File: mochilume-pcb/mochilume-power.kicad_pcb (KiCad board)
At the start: 2 copper layers, 90 x 60.1 mm, 28 parts, among them U1 llcc68_custom_module

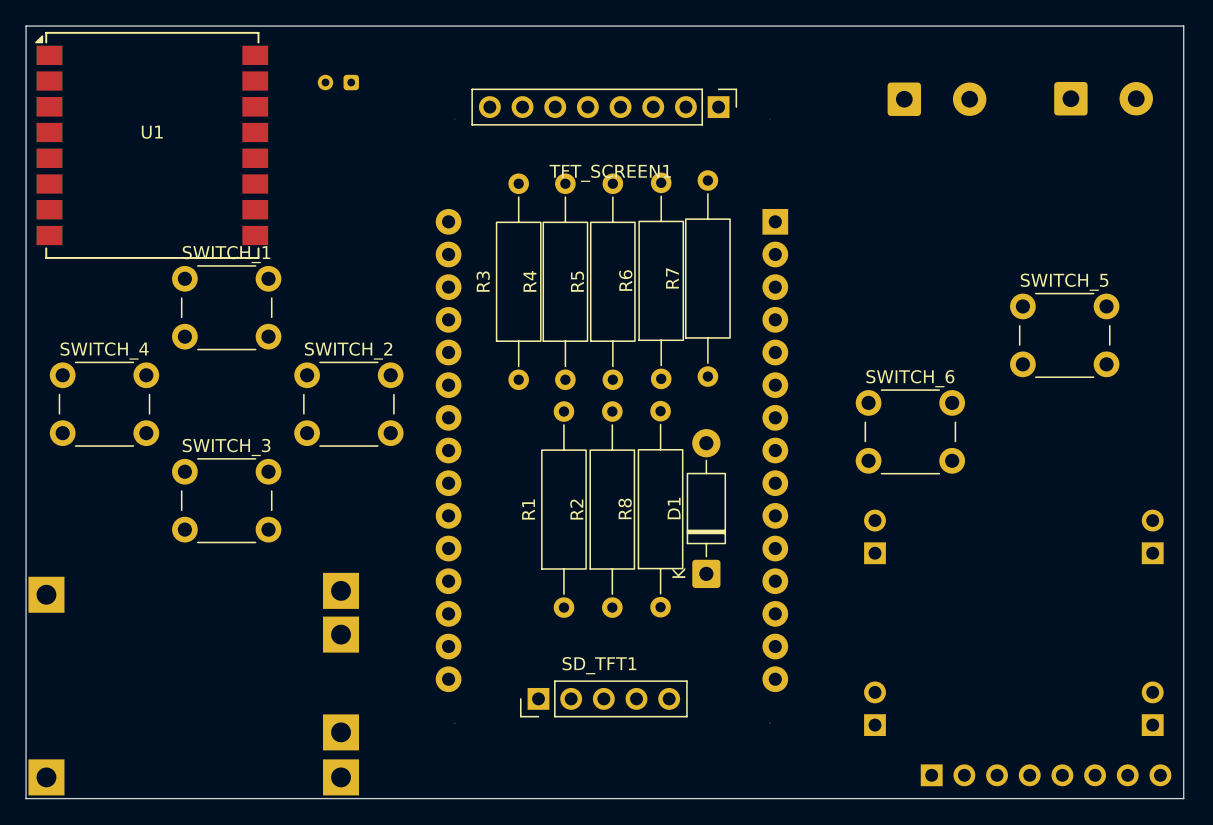
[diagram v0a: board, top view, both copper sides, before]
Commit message: feat pcb: add via tracking to power pcb
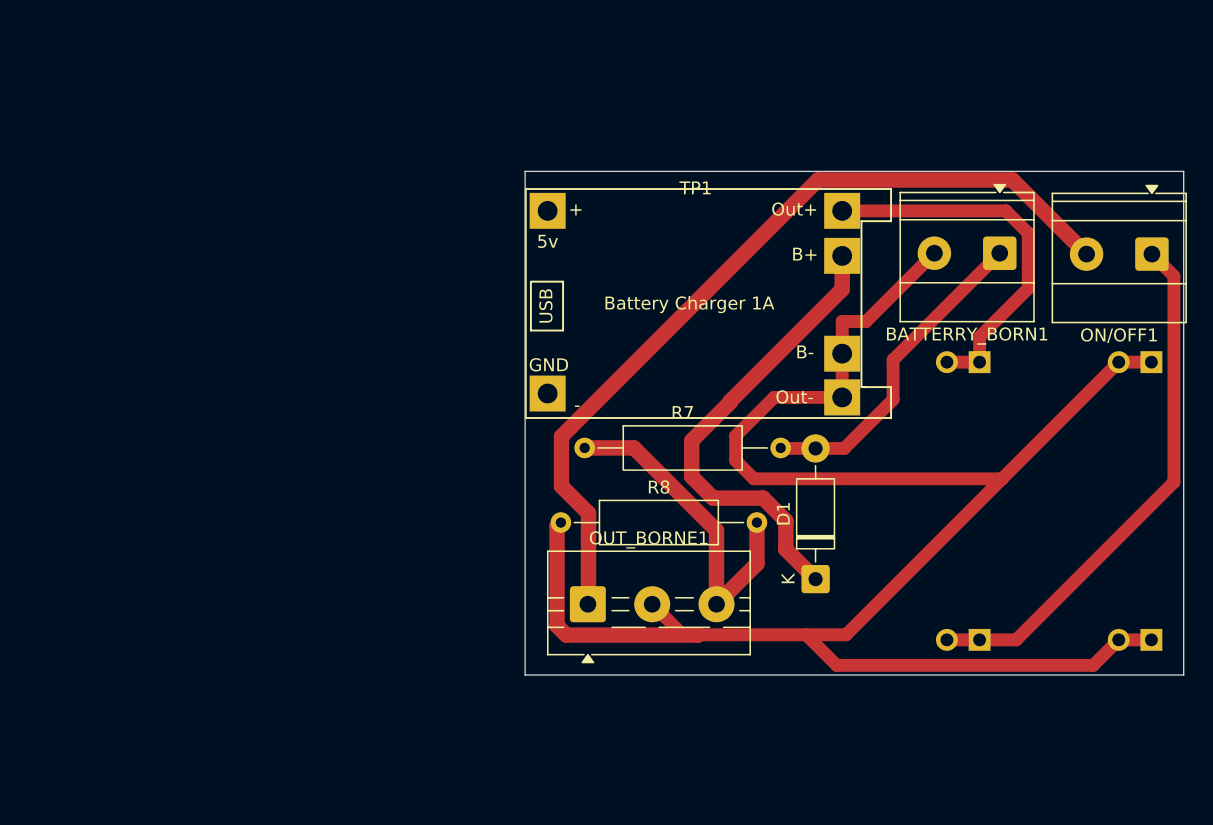
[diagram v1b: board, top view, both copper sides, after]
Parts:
- removed ACCELEROMETER1, TFT_SCREEN1: ~, Connector_PinHeader_2.54mm:PinHeader_1x08_P2.54mm_Vertical
- removed C1: 10uF, Capacitor_THT:CP_Radial_D4.0mm_P2.00mm
- removed ESP32-WROOM-DEVKIT-V1: ~, Library:MODULE_ESP32_DEVKIT_V1
- removed R1, R2, R3, R4, R5, R6: 10K, Resistor_THT:R_Axial_DIN0309_L9.0mm_D3.2mm_P15.24mm_Horizontal
- removed SD_TFT1: ~, Connector_PinHeader_2.54mm:PinHeader_1x05_P2.54mm_Vertical
- removed SWITCH_1, SWITCH_2, SWITCH_3, SWITCH_4, SWITCH_5, SWITCH_6: ~, Button_Switch_THT:SW_PUSH_6mm
- removed U1: llcc68_custom_module, RF_Module:Ai-Thinker-Ra-01-LoRa
- added OUT_BORNE1: Screw_Terminal_01x03, TerminalBlock:TerminalBlock_MaiXu_MX126-5.0-03P_1x03_P5.00mm, F.Cu at (216.7, 127.7)
- BATTERRY_BORN1, ON/OFF1, TP1: moved to F.Cu
- moved TP1 61.4 mm to (211.8, 95.4)
- moved GND1 28.2 mm to (260.5, 108.8), turned to 90 degrees
- moved ON/OFF1 22.7 mm to (260.5, 100.4), turned to 180 degrees
- moved GNDIN1 22.5 mm to (260.5, 130.4), turned to 90 degrees
- moved VIN1 16.9 mm to (247.1, 108.8), turned to 90 degrees
- moved VOUT1 15.1 mm to (247.1, 130.4), turned to 90 degrees
- moved BATTERRY_BORN1 13.2 mm to (248.7, 100.4), turned to 180 degrees
- moved R7 11.1 mm to (216.4, 115.5), turned to 0 degrees
- moved R8 10.2 mm to (214.6, 121.3), turned to 0 degrees
- moved D1 8.50 mm to (234.4, 125.7)
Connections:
- TP1 pad 1: ESP_VIN -> unconnected-(TP1-VIN-Pad1)
- TP1 pad 2: GND -> unconnected-(TP1-GNDIN-Pad2)
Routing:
- net GND: track 0.00 -> 144.7 mm
- net VCC: track 0.00 -> 65.4 mm
- net VCC_IN: track 0.00 -> 41.2 mm
- net Net-(D1-K): track 0.00 -> 36.2 mm
- net VIN: track 0.00 -> 29.3 mm
- net BATERIA: track 0.00 -> 26.3 mm
- net BATTERY +: track 0.00 -> 25.1 mm
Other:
- board size 90 x 60.1 mm -> 51.2 x 39.2 mm

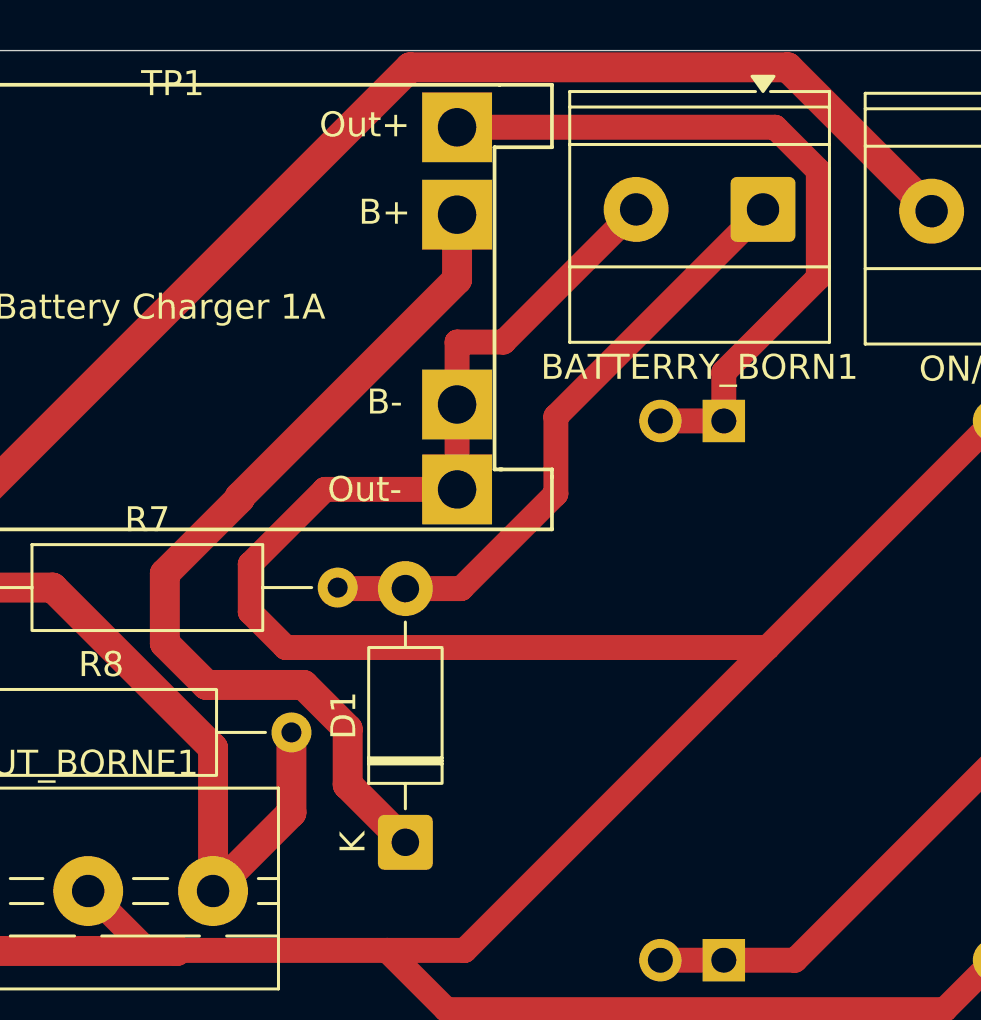
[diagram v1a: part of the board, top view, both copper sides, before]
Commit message: fix power pcb: remove diode that disable tpu4056
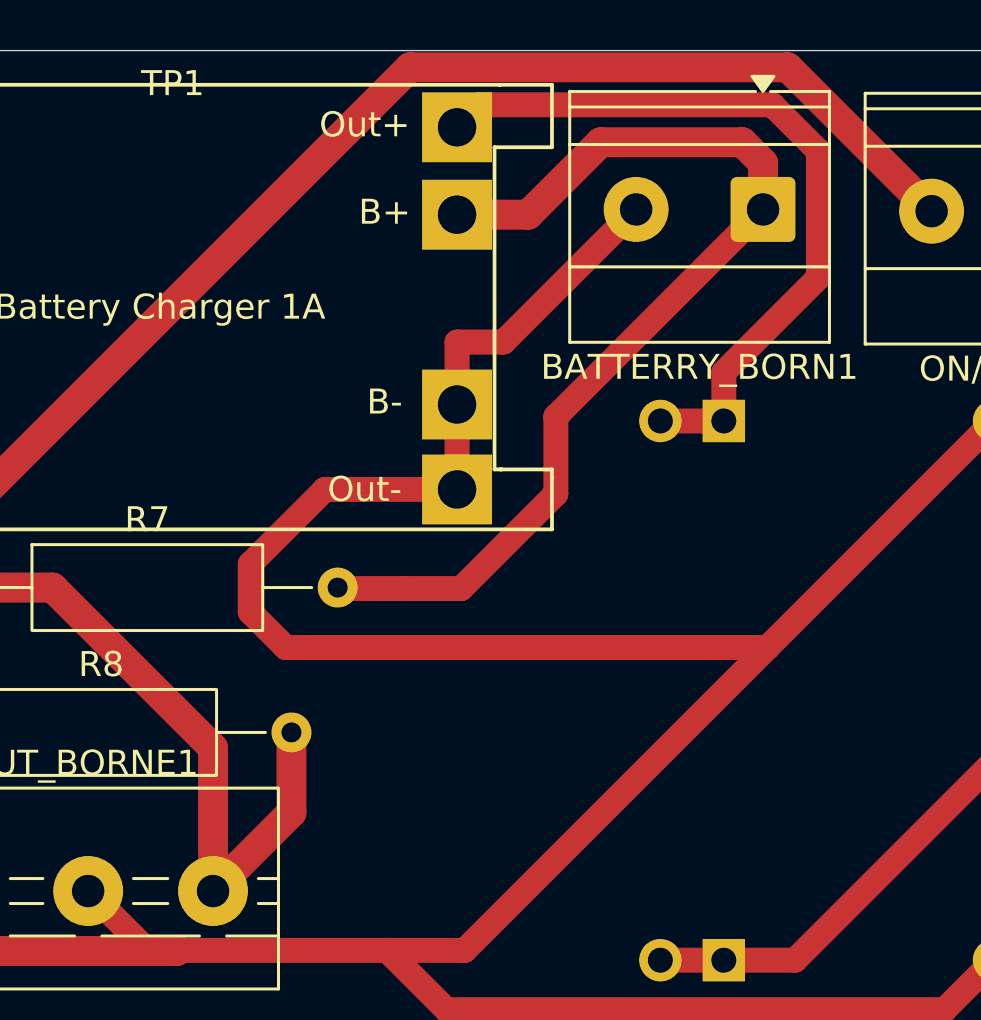
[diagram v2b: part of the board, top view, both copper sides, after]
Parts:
- removed D1: 1N5819, Diode_THT:D_DO-41_SOD81_P10.16mm_Horizontal
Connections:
- TP1 pad 5: Net-(D1-K) -> BATTERY +
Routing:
- net Net-(D1-K): track 36.2 -> 0.00 mm
- net BATTERY +: track 25.1 -> 40.8 mm
- net VIN: track 29.3 -> 30.5 mm
